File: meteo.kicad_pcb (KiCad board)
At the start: 2 copper layers, 165.2 x 119.2 mm, 26 parts, among them J1 mlab I2C, J10 Eth, J11 I2C0, J12 I2C1, J13 I2C2, J14 I2C3, J15 UART, J16 UART pow, J17 5V jumper, J18 power control circuit, J2 SPI, J3 Analog, J4 Conn_02x19_Odd_Even, J5 Conn_02x18_Odd_Even, J6 I/O, J9 SD, U1 CD74HC4067M, U2 CD74HC4067M, U3 multiplex analog, U4 ADS1015IDGS, U5 PCF8575DBR

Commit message: Uploading newer version
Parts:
- added R3: R, Resistor_THT:R_Axial_DIN0207_L6.3mm_D2.5mm_P15.24mm_Horizontal, F.Cu at (137.1, 129.5)
- added R4: R, Resistor_THT:R_Axial_DIN0207_L6.3mm_D2.5mm_P15.24mm_Horizontal, F.Cu at (134.6, 126.5)
- J10: moved to F.Cu
- moved J10 33.9 mm to (112.4, 135.1)
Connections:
- J18 pad 1: 5V -> HW_reset
- J18 pad 3: HW_reset -> 5V
- U1 pad 15: unconnected-(U1-~{E}-Pad15) -> GND
- U2 pad 15: unconnected-(U2-~{E}-Pad15) -> GND
- U3 pad 15: unconnected-(U3-~{E}-Pad15) -> GND
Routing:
- net 5V: track 520.9 -> 575.0 mm
- net +3.3V: track 51.1 -> 56.9 mm
- net MISO: track 96.0 -> 91.1 mm
- net SCK: track 113.1 -> 109.3 mm
- net SDA: track 208.9 -> 212.3 mm
- net CS0: track 41.4 -> 44.6 mm
- net SCL: track 201.1 -> 204.1 mm
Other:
- outline, holes or cut-outs redrawn

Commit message: Adding pins for power and pullup ressistors for I2C
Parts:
- added J7: mlab_pow, Connector_PinSocket_2.54mm:PinSocket_2x03_P2.54mm_Vertical, F.Cu at (165.6, 186.7)
- moved J17 5.10 mm to (75.9, 185.0), turned to 180 degrees
- moved J18 0.05 mm to (71.6, 179.9)
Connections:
- U4 pad 1: unconnected-(U4-ADDR-Pad1) -> GND
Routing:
- net GND: track 29.8 -> 0.00 mm
- net 5V: track 575.0 -> 566.2 mm
- net HW_reset: track 52.8 -> 50.6 mm
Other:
- board text added: "POWER"
- board text added: "POWER control"
- board text removed: "POW"

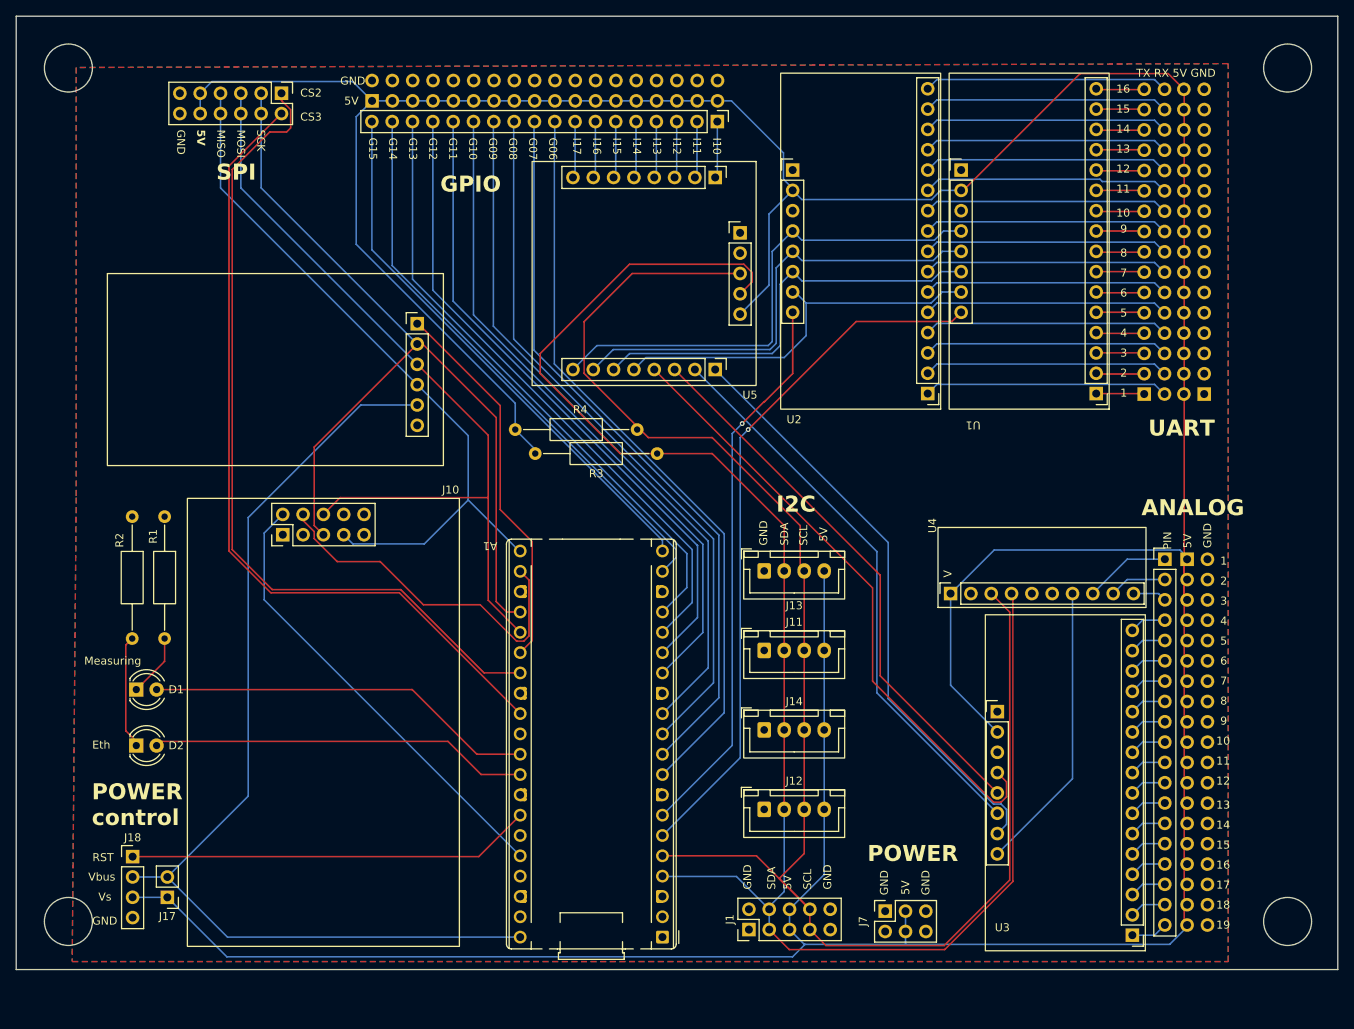
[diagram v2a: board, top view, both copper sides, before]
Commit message: fixing footprints
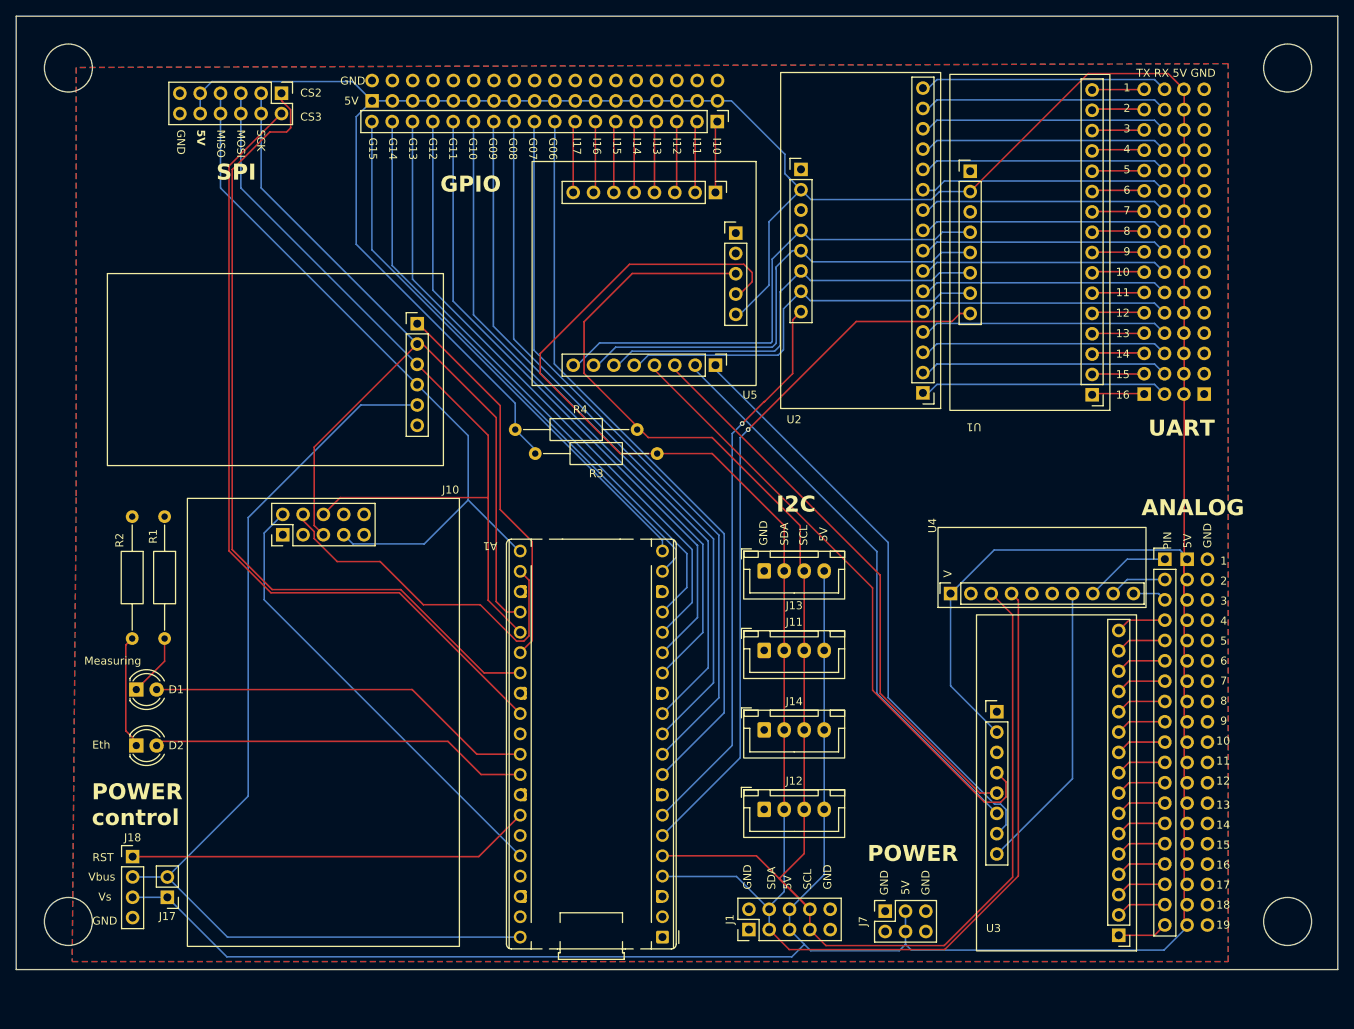
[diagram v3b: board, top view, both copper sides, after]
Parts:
- moved U3 1.11 mm to (177.0, 191.7)
- moved U1 0.25 mm to (173.7, 124.2)
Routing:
- net Net-(J6-Pin_4): track 6.72 -> 8.96 mm
- net Net-(J6-Pin_7): track 6.72 -> 8.96 mm
- net Net-(J6-Pin_3): track 6.72 -> 8.96 mm
- net Net-(J6-Pin_8): track 6.72 -> 8.96 mm
- net Net-(J6-Pin_6): track 6.72 -> 8.96 mm
- net Net-(J6-Pin_5): track 6.72 -> 8.96 mm
- net Net-(J6-Pin_1): track 6.72 -> 8.96 mm
- net Net-(J6-Pin_2): track 6.80 -> 8.96 mm
- net Net-(J3-Pin_8): track 4.59 -> 6.30 mm
- net Net-(J3-Pin_5): track 4.59 -> 6.30 mm
- net Net-(J3-Pin_19): track 4.59 -> 6.30 mm
- net Net-(J3-Pin_15): track 4.59 -> 6.30 mm
- net Net-(J3-Pin_12): track 4.59 -> 6.30 mm
- net Net-(J3-Pin_7): track 4.59 -> 6.30 mm
- net Net-(J3-Pin_4): track 4.59 -> 6.30 mm
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
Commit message: Oprava děr
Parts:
- added H1: MountingHole_Pad, MountingHole:MountingHole_3.2mm_M3_DIN965_Pad, F.Cu at (213.4, 81.3)
- added H2: MountingHole_Pad, MountingHole:MountingHole_3.2mm_M3_DIN965_Pad, F.Cu at (213.4, 193.0)
- added H3: MountingHole_Pad, MountingHole:MountingHole_3.2mm_M3_DIN965_Pad, F.Cu at (63.5, 193.0)
- added H4: MountingHole_Pad, MountingHole:MountingHole_3.2mm_M3_DIN965_Pad, F.Cu at (63.5, 81.3)
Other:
- board size 165.2 x 119.2 mm -> 161.2 x 124.5 mm
